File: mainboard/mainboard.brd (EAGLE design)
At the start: 158.8 x 136.4 mm, 53 parts, among them T2 NPN_BC817,215, X1 JST-XH-06-PIN-LONG-PAD

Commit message: Adding multiplexer on mainboard, sampling charge current, separate com ces
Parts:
- added C4: 1000pF, SparkFun-Passives:0805@1
- added R20: 2K, SparkFun-Resistors:0805
- added R21: 3K, SparkFun-Resistors:0805
- added SENSE: ACS712, rhoban:SO8
- added U1: CD4051BM, rhoban:SOIC127P600X175-16N
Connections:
- new net ADDR1: MAPLE.X14, U1.11
- new net ADDR2: U1.10
- new net ADDR3: MAPLE.X2, U1.9
- new net ADDR4: MAPLE.X31
- new net CHARGE_CUR: R20.2, R21.1, U1.2
- new net COM_CE1: COM1.CE
- new net COM_CE2: COM2.CE, MAPLE.X3
- new net COM_CE3: COM3.CE, MAPLE.X9
- new net MUX: MAPLE.X8, U1.3
- new net N$24: R20.1, SENSE.7
- new net N$26: U1.4
- new net N$27: C4.1, SENSE.6
- new net VIN_KICKER: SENSE.1, SENSE.2, X1.2
- net 3.3: now also U1.16
- net BAT: now also U1.5; no longer MAPLE.X9
- net CAP: now also U1.1; no longer MAPLE.X3
- net COM_CE: no longer COM1.CE, COM2.CE, COM3.CE
- net GND: now also C4.2, R21.2, SENSE.5, U1.6, U1.7, U1.8
- net HALL1: now also U1.13; no longer MAPLE.X14
- net HALL2: now also U1.14; no longer MAPLE.X8
- net HALL3: now also U1.15; no longer MAPLE.X2
- net HALL4: now also U1.12; no longer MAPLE.X31
- net VCC: now also SENSE.8
- net VIN: now also SENSE.3, SENSE.4; no longer X1.2
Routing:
- net GND: track 161.0 -> 167.2 mm, vias 0 -> 1

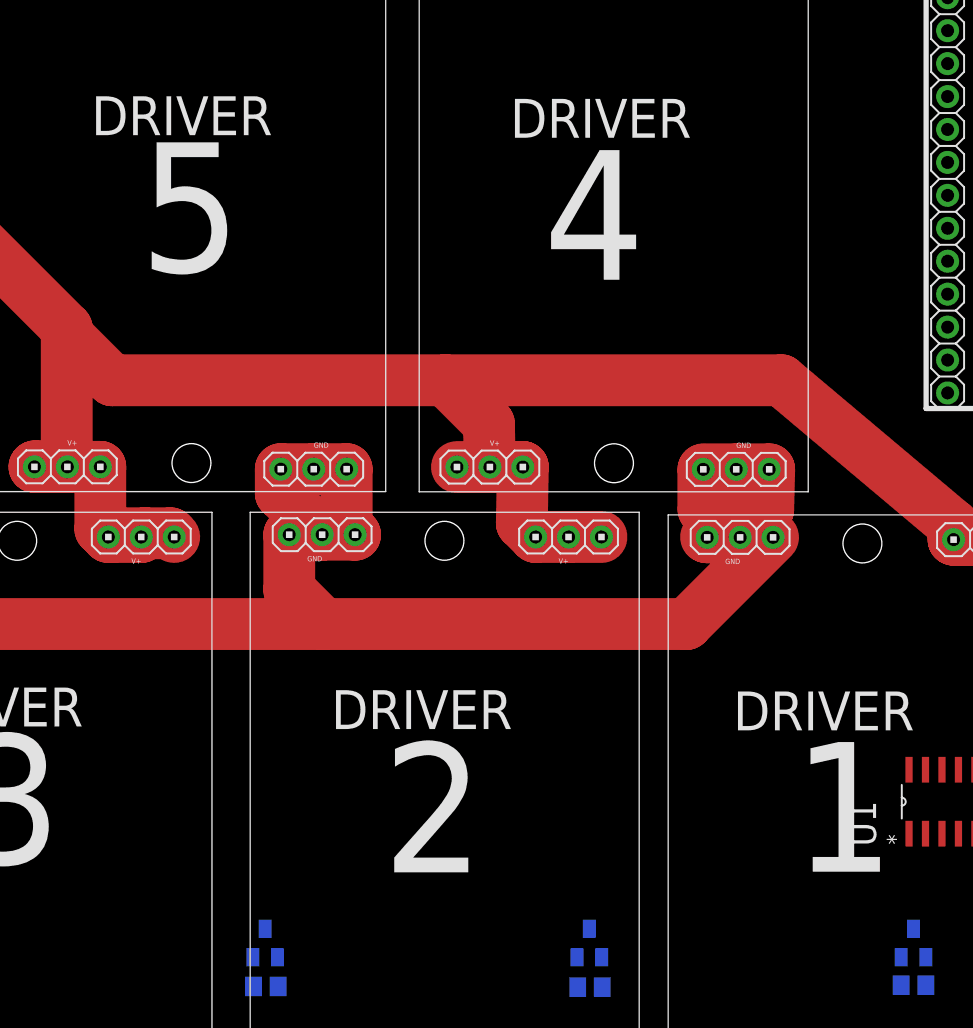
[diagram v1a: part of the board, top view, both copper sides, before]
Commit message: Fixing mux addr, drivers #
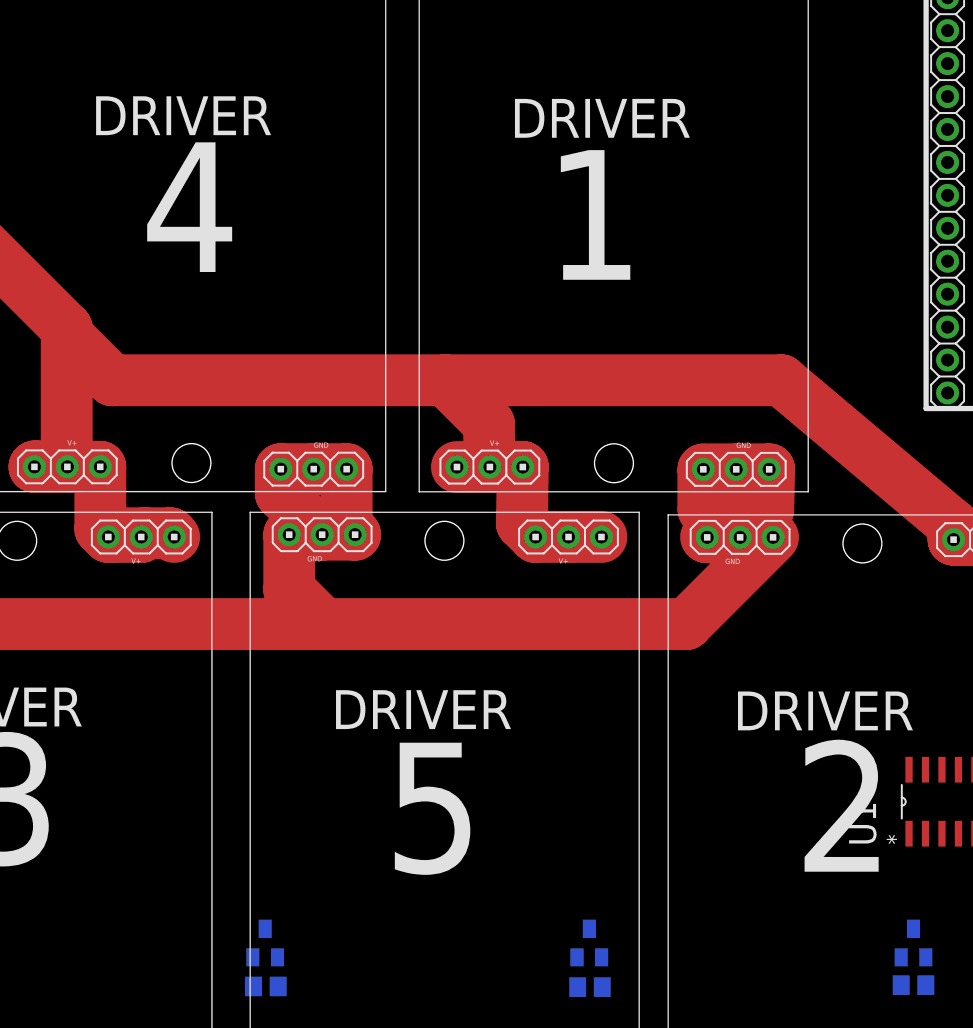
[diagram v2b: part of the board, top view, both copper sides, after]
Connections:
- removed net ADDR4: MAPLE.X31
- net ADDR2: now also MAPLE.X31
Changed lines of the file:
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@@
 <dimension x1="-59.75" y1="43.75" x2="-59.75" y2="-38.25" x3="-102.750009375" y3="2.75" layer="51"/>
 <dimension x1="1.7" y1="60.8" x2="2" y2="-77.5" x3="111.65133125" y3="-8.11181875" layer="51"/>
-<text x="38.050003125" y="-21.8" size="10" layer="112" rot="R180">1</text>
-<text x="6.4" y="-21.85" size="10" layer="112" rot="R180">2</text>
-<text x="-12.35" y="24.45" size="10" layer="112" rot="R180">5</text>
+<text x="38.050003125" y="-21.8" size="10" layer="112" rot="R180">2</text>
+<text x="6.4" y="-21.85" size="10" layer="112" rot="R180">5</text>
+<text x="-12.35" y="24.45" size="10" layer="112" rot="R180">4</text>
 <text x="-26.2" y="-21.2" size="10" layer="112" rot="R180">3</text>
-<text x="18.8" y="23.85" size="10" layer="112" rot="R180">4</text>
+<text x="18.8" y="23.85" size="10" layer="112" rot="R180">1</text>
 <text x="-55.25" y="-14" size="1.778" layer="121">3.3V</text>
 <text x="-54.5" y="-23.5" size="1.778" layer="121">5V</text>
@@
 <signal name="ADDR2">
 <contactref element="U1" pad="10"/>
+<contactref element="MAPLE" pad="X31"/>
+<wire x1="46.774915625" y1="-23.936146875" x2="42.13" y2="5.12" width="0" layer="19" extent="1-1"/>
 </signal>
 <signal name="ADDR3">
@@
 <contactref element="U1" pad="4"/>
 </signal>
-<signal name="ADDR4">
-<contactref element="MAPLE" pad="X31"/>
-</signal>
 <signal name="COM_CE1">

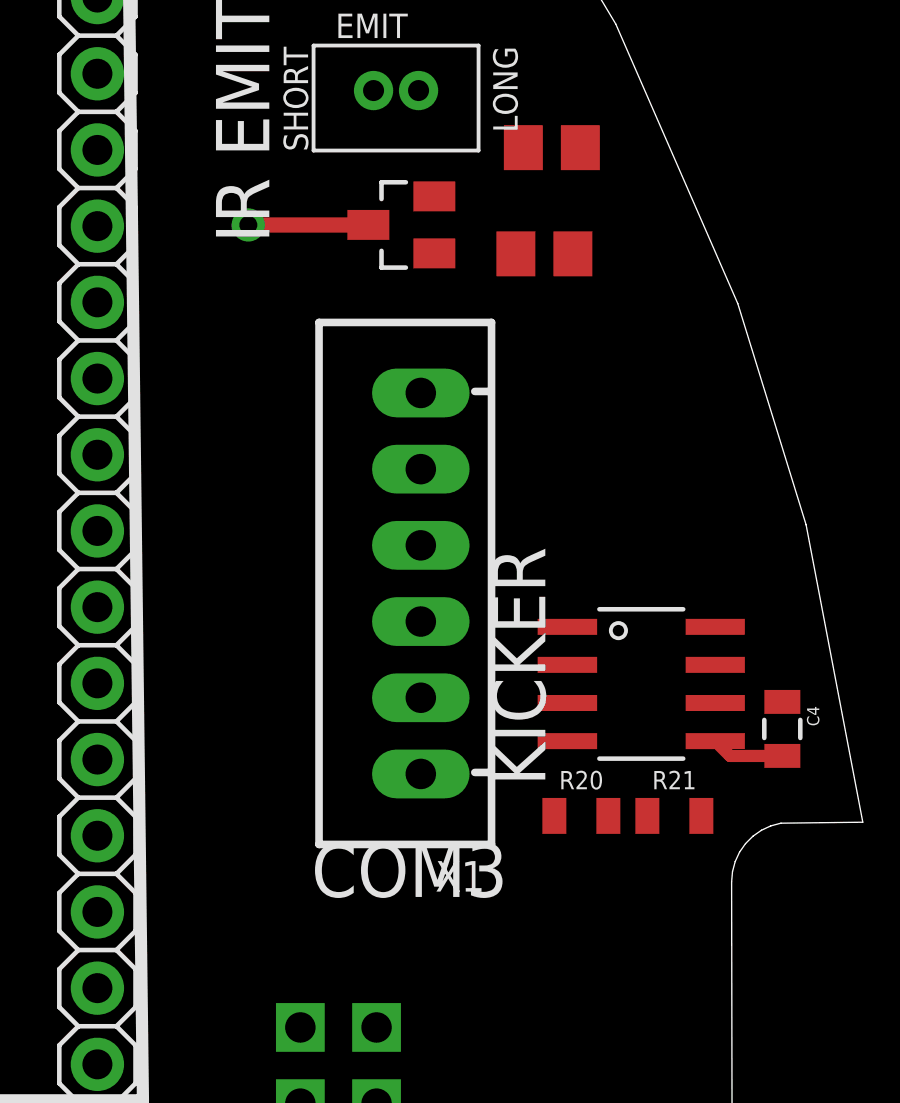
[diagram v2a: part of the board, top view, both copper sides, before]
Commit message: Using mos driver on kicker board
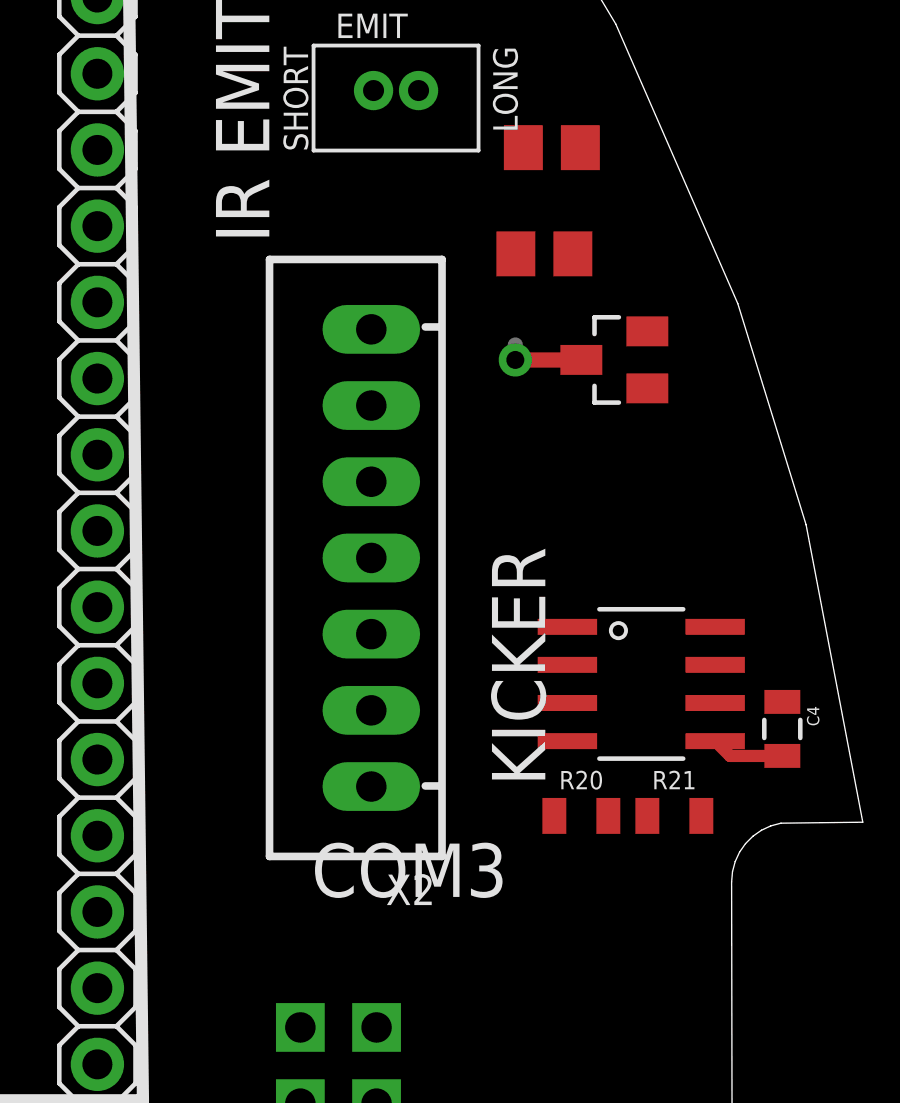
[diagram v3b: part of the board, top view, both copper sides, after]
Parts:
- removed X1: JST-XH-06-PIN-LONG-PAD, Rembrandt Electronics - JST XH Connectors v1-0:JST-XH-06-PACKAGE-LONG-PAD
- added X2: JST-XH-07-PIN-LONG-PAD, Rembrandt Electronics - JST XH Connectors v1-0:JST-XH-07-PACKAGE-LONG-PAD
- moved T2 8.41 mm to (74.6, 28.6)
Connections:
- net 12V: now also X2.3
- net BOOST_EN: now also X2.4; no longer X1.3
- net CAP: now also X2.7; no longer X1.6
- net GND: now also X2.1; no longer X1.1
- net KICK1: now also X2.5; no longer X1.4
- net KICK2: now also X2.6; no longer X1.5
- net VIN_KICKER: now also X2.2; no longer X1.2
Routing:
- net N$7: track 4.40 -> 2.70 mm
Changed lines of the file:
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@@
 <attribute name="FARNELL" value="3152856" x="-60.61493125" y="36.5450375" size="1.778" layer="27" display="off"/>
 </element>
-<element name="T2" library="rhoban" package="SOT-23" value="NPN_BC817,215" x="67.49994375" y="33.10006875" rot="R90">
-<attribute name="FARNELL" value="1081223" x="67.49994375" y="33.10006875" size="1.778" layer="27" rot="R90" display="off"/>
+<element name="T2" library="rhoban" package="SOT-23" value="NPN_BC817,215" x="74.599925" y="28.600078125" rot="R90">
+<attribute name="FARNELL" value="1081223" x="74.599925" y="28.600078125" size="1.778" layer="27" rot="R90" display="off"/>
 </element>
 <element name="R4" library="rhoban" package="R0805" value="1K" x="72.269928125" y="32.135040625" rot="R180">
@@
 <element name="U$7" library="rhoban" package="PANASONIC_D8" value="220uF" x="-62.950071875" y="17.25001875" rot="R180">
 <attribute name="FARNELL" value="1850103" x="-62.950071875" y="17.25001875" size="1.778" layer="27" rot="R180" display="off"/>
-</element>
-<element name="X1" library="Rembrandt Electronics - JST XH Connectors v1-0" package="JST-XH-06-PACKAGE-LONG-PAD" value="JST-XH-06-PIN-LONG-PAD" x="68.149975" y="21.149953125" rot="R90">
-<attribute name="FARNELL" value="-" x="68.149975" y="21.149953125" size="1.778" layer="27" rot="R90" display="off"/>
 </element>
 <element name="U$8" library="rhoban" package="PANASONIC_D8" value="220uF" x="65.550075" y="-10.1000125">
@@
 <attribute name="VALUE" value=" " x="70.799859375" y="9.89998125" size="1.778" layer="27" display="off"/>
 </element>
+<element name="X2" library="Rembrandt Electronics - JST XH Connectors v1-0" package="JST-XH-07-PACKAGE-LONG-PAD" value="JST-XH-07-PIN-LONG-PAD" x="66.49986875" y="21.999959375" rot="R90"/>
 </elements>
 <signals>
 <signal name="KICK2">
-<contactref element="X1" pad="5"/>
 <contactref element="MAPLE" pad="X26"/>
-<wire x1="42.13" y1="17.82" x2="68.149975" y2="24.959953125" width="0" layer="19" extent="1-1"/>
+<contactref element="X2" pad="6"/>
+<wire x1="42.13" y1="17.82" x2="66.49986875" y2="27.079959375" width="0" layer="19" extent="1-1"/>
 </signal>
 <signal name="3.3" class="1">
@@
 <contactref element="U$8" pad="-"/>
 <contactref element="U$9" pad="-"/>
-<contactref element="X1" pad="1"/>
 <contactref element="U$1" pad="3"/>
 <contactref element="U$5" pad="3"/>
@@
 <contactref element="C4" pad="2"/>
 <contactref element="R21" pad="2"/>
+<wire x1="-60.84493125" y1="36.5450375" x2="-64.499871875" y2="36.5450375" width="0.4064" layer="1"/>
+<wire x1="-64.499871875" y1="36.5450375" x2="-64.499871875" y2="36.599928125" width="0.4064" layer="1"/>
+<via x="-64.499871875" y="36.599928125" extent="1-16" drill="0.6" shape="square"/>
+<wire x1="-64.499871875" y1="36.599928125" x2="-64.499871875" y2="36.499928125" width="0.4064" layer="16"/>
+<wire x1="77.96365" y1="15.894965625" x2="78.45864375" y2="15.399971875" width="0.4064" layer="1"/>
+<wire x1="78.45864375" y1="15.399971875" x2="80.199840625" y2="15.399971875" width="0.4064" layer="1"/>
+<contactref element="X2" pad="1"/>
 <wire x1="42.13" y1="50.84" x2="57.37" y2="50.84" width="0" layer="19" extent="1-1"/>
-<wire x1="68.59994375" y1="34.05006875" x2="57.37" y2="50.84" width="0" layer="19" extent="1-1"/>
-<wire x1="68.149975" y1="14.799953125" x2="68.59994375" y2="34.05006875" width="0" layer="19" extent="1-1"/>
-<wire x1="77.499846875" y1="13.399975" x2="68.149975" y2="14.799953125" width="0" layer="19" extent="1-1"/>
-<wire x1="77.96365" y1="15.894965625" x2="77.499846875" y2="13.399975" width="0" layer="19" extent="1-1"/>
-<wire x1="64.135" y1="-1.27" x2="68.149975" y2="14.799953125" width="0" layer="19" extent="1-1"/>
+<wire x1="75.699925" y1="29.550078125" x2="57.37" y2="50.84" width="0" layer="19" extent="1-1"/>
+<wire x1="77.96365" y1="15.894965625" x2="75.699925" y2="29.550078125" width="0" layer="19" extent="1-1"/>
+<wire x1="77.499846875" y1="13.399975" x2="78.45864375" y2="15.399971875" width="0" layer="19" extent="1-1"/>
+<wire x1="66.49986875" y1="14.379959375" x2="77.499846875" y2="13.399975" width="0" layer="19" extent="1-1"/>
+<wire x1="64.135" y1="-1.27" x2="66.49986875" y2="14.379959375" width="0" layer="19" extent="1-1"/>
 <wire x1="62.820075" y1="-10.1000125" x2="64.135" y2="-1.27" width="0" layer="19" extent="1-1"/>
 <wire x1="67.099746875" y1="-15.49990625" x2="62.820075" y2="-10.1000125" width="0" layer="19" extent="1-1"/>
@@
 <wire x1="-66.09" y1="-11.71" x2="-69.18" y2="-17.635" width="0" layer="19" extent="1-1"/>
 <wire x1="-69.405" y1="-10.49" x2="-66.09" y2="-11.71" width="0" layer="19" extent="1-1"/>
+<wire x1="-60.84493125" y1="36.5450375" x2="-60.220071875" y2="17.25001875" width="0" layer="19" extent="1-1"/>
 <wire x1="8.972815625" y1="44.012825" x2="42.13" y2="50.84" width="0" layer="19" extent="1-1"/>
 <wire x1="-6.60005" y1="53.745025" x2="8.972815625" y2="44.012825" width="0" layer="19" extent="1-1"/>
 <wire x1="-23.6122" y1="44.0278" x2="-6.60005" y2="53.745025" width="0" layer="19" extent="1-1"/>
-<wire x1="-60.84493125" y1="36.5450375" x2="-64.499871875" y2="36.5450375" width="0.4064" layer="1"/>
-<wire x1="-64.499871875" y1="36.5450375" x2="-64.499871875" y2="36.599928125" width="0.4064" layer="1"/>
-<via x="-64.499871875" y="36.599928125" extent="1-16" drill="0.6" shape="square"/>
-<wire x1="-64.499871875" y1="36.599928125" x2="-64.499871875" y2="36.499928125" width="0.4064" layer="16"/>
-<wire x1="-64.499871875" y1="36.499928125" x2="-60.220071875" y2="17.25001875" width="0" layer="19" extent="1-16"/>
-<wire x1="77.96365" y1="15.894965625" x2="78.45864375" y2="15.399971875" width="0.4064" layer="1"/>
-<wire x1="78.45864375" y1="15.399971875" x2="80.199840625" y2="15.399971875" width="0.4064" layer="1"/>
 </signal>
 <signal name="VIN" class="2">
@@
 </signal>
 <signal name="KICK1">
-<contactref element="X1" pad="4"/>
 <contactref element="MAPLE" pad="X25"/>
-<wire x1="42.13" y1="20.36" x2="68.149975" y2="22.419953125" width="0" layer="19" extent="1-1"/>
+<contactref element="X2" pad="5"/>
+<wire x1="42.13" y1="20.36" x2="66.49986875" y2="24.539959375" width="0" layer="19" extent="1-1"/>
 </signal>
 <signal name="BOOST_EN">
 <contactref element="MAPLE" pad="X27"/>
-<contactref element="X1" pad="3"/>
-<wire x1="42.13" y1="15.28" x2="68.149975" y2="19.879953125" width="0" layer="19" extent="1-1"/>
+<contactref element="X2" pad="4"/>
+<wire x1="42.13" y1="15.28" x2="66.49986875" y2="21.999959375" width="0" layer="19" extent="1-1"/>
 </signal>
 <signal name="CAP">
-<contactref element="X1" pad="6"/>
 <contactref element="U1" pad="1"/>
-<wire x1="39.154915625" y1="-28.863746875" x2="68.149975" y2="27.499953125" width="0" layer="19" extent="1-1"/>
+<contactref element="X2" pad="7"/>
+<wire x1="39.154915625" y1="-28.863746875" x2="66.49986875" y2="29.619959375" width="0" layer="19" extent="1-1"/>
 </signal>
 <signal name="N$3">
@@
 <contactref element="EMIT" pad="P$2"/>
 <contactref element="T2" pad="3"/>
-<wire x1="66.39994375" y1="33.10006875" x2="62.39994375" y2="33.10006875" width="0.508" layer="1"/>
-<via x="62.39994375" y="33.10006875" extent="1-16" drill="0.6" shape="square"/>
-<wire x1="62.39994375" y1="33.10006875" x2="62.09994375" y2="33.10006875" width="0.508" layer="16"/>
-<wire x1="62.09994375" y1="33.10006875" x2="62.09994375" y2="33.00006875" width="0.508" layer="16"/>
-<wire x1="66.39994375" y1="33.10006875" x2="66.574928125" y2="37.580040625" width="0" layer="19" extent="1-1"/>
+<wire x1="73.499925" y1="28.600078125" x2="71.299925" y2="28.600078125" width="0.508" layer="1"/>
+<via x="71.299925" y="28.600078125" extent="1-16" drill="0.6" shape="square"/>
+<wire x1="71.299925" y1="28.600078125" x2="71.299925" y2="29.100075" width="0.508" layer="16"/>
+<wire x1="71.299925" y1="29.100075" x2="66.574928125" y2="37.580040625" width="0" layer="19" extent="16-16"/>
 </signal>
 <signal name="N$11">
 <contactref element="T2" pad="1"/>
 <contactref element="R4" pad="2"/>
-<wire x1="68.59994375" y1="32.15006875" x2="71.319928125" y2="32.135040625" width="0" layer="19" extent="1-1"/>
+<wire x1="71.319928125" y1="32.135040625" x2="75.699925" y2="27.650078125" width="0" layer="19" extent="1-1"/>
 </signal>
 <signal name="DRIVERS_MOSI">
@@
 <contactref element="MAPLE" pad="X13"/>
 </signal>
-<signal name="12V" class="1">
+<signal name="12V">
 <contactref element="U$6" pad="+"/>
 <contactref element="C2" pad="2"/>
@@
 <contactref element="D4" pad="2"/>
 <contactref element="D3" pad="2"/>
+<contactref element="X2" pad="3"/>
 <wire x1="-61.35" y1="-27.5" x2="-69.05" y2="-23.1" width="0" layer="19" extent="1-1"/>
 <wire x1="-55.33" y1="-27.75" x2="-61.35" y2="-27.5" width="0" layer="19" extent="1-1"/>
@@
 <wire x1="4.13" y1="-46.005" x2="-28.77" y2="-46.105" width="0" layer="19" extent="1-1"/>
 <wire x1="36.465" y1="-45.96" x2="4.13" y2="-46.005" width="0" layer="19" extent="1-1"/>
-<wire x1="-16.99" y1="39.59" x2="-55.33" y2="-27.75" width="0" layer="19" extent="1-1"/>
-<wire x1="15.52" y1="39.41" x2="-16.99" y2="39.59" width="0" layer="19" extent="1-1"/>
+<wire x1="66.49986875" y1="19.459959375" x2="36.465" y2="-45.96" width="0" layer="19" extent="1-1"/>
+<wire x1="15.52" y1="39.41" x2="66.49986875" y2="19.459959375" width="0" layer="19" extent="1-1"/>
+<wire x1="-16.99" y1="39.59" x2="15.52" y2="39.41" width="0" layer="19" extent="1-1"/>
 </signal>
 <signal name="BAT">
@@
 <contactref element="SENSE" pad="1"/>
 <contactref element="SENSE" pad="2"/>
-<contactref element="X1" pad="2"/>
+<contactref element="X2" pad="2"/>
 <wire x1="73.03605" y1="18.434965625" x2="73.03605" y2="19.704965625" width="0" layer="19" extent="1-1"/>
-<wire x1="68.149975" y1="17.339953125" x2="73.03605" y2="18.434965625" width="0" layer="19" extent="1-1"/>
+<wire x1="66.49986875" y1="16.919959375" x2="73.03605" y2="18.434965625" width="0" layer="19" extent="1-1"/>
 </signal>
 </signals>
